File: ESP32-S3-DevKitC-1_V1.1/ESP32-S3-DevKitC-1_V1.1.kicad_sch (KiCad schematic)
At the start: 46 parts, among them IC1 SGM2212-3.3XKC3G_TR, J2 Conn_01x22, J3 Conn_01x22, P1 USB_C_Plug_USB2.0, Q3 L8050QLT1G, Q4 L8050QLT1G, SW1 NTC013-AT1J-A160T, SW2 NTC013-AT1J-A160T, U1 CP2102N-Axx-xQFN28, U4 ESP32-S3-WROOM-1, U5 AMS1117

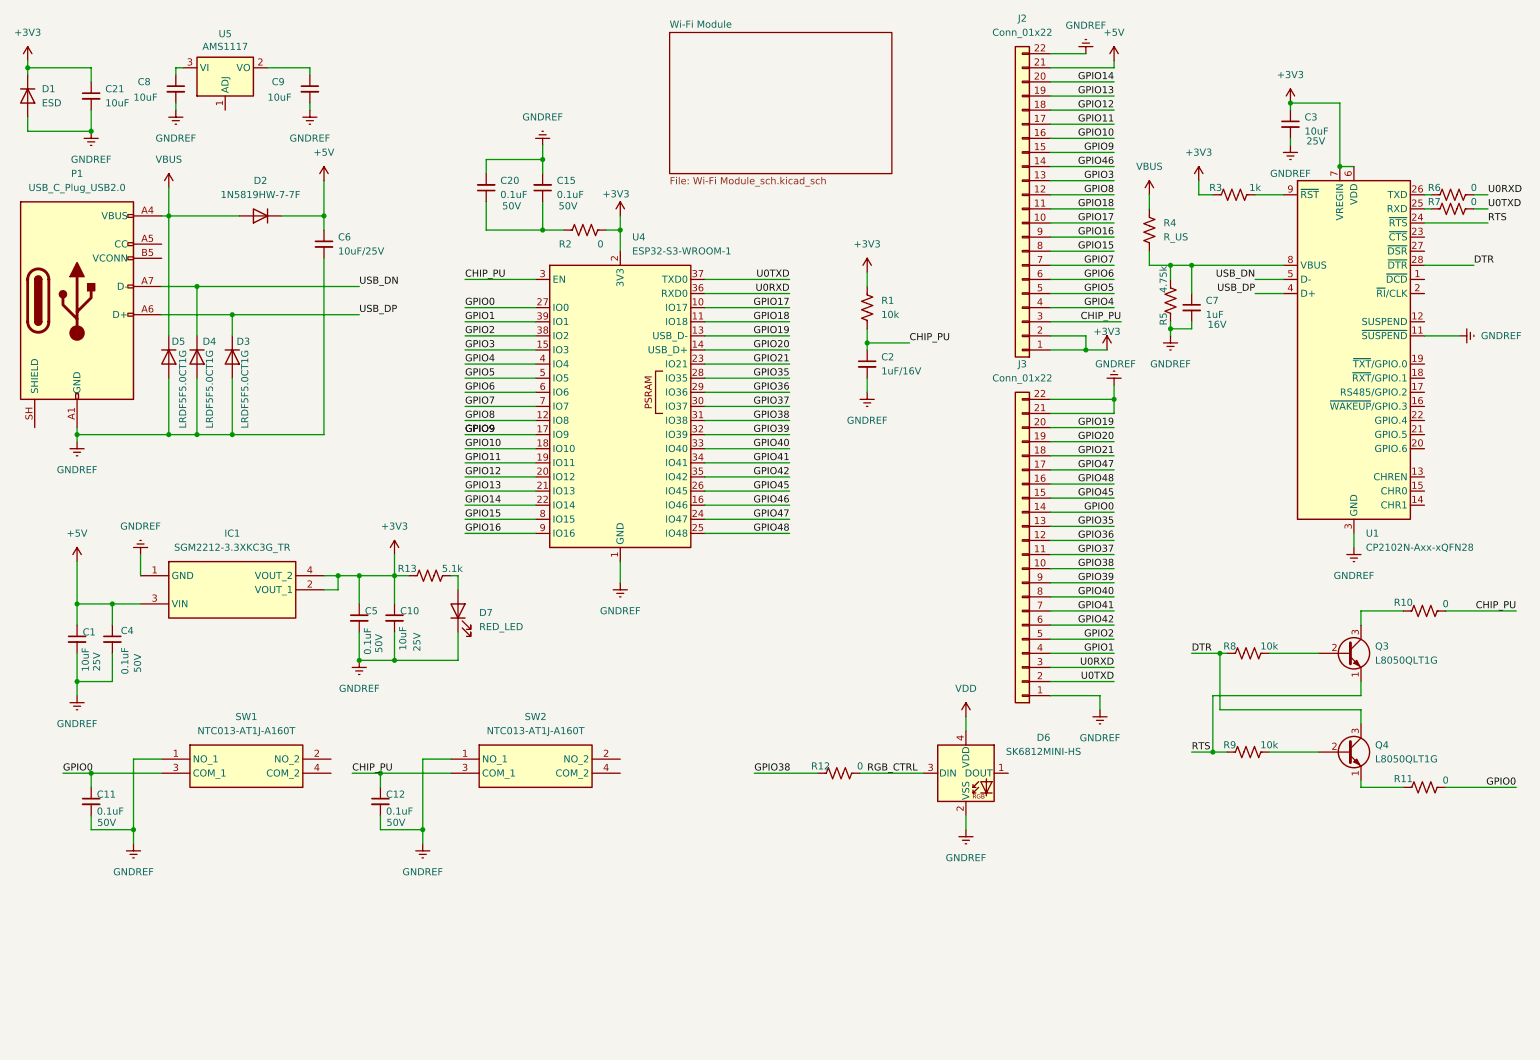
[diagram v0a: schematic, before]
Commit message: Update ESP32-S3-DevKitC-1_V1.1
I'm update the ESP32-S3-DevKitC-1_V1.1, include the sch and pcb layout.
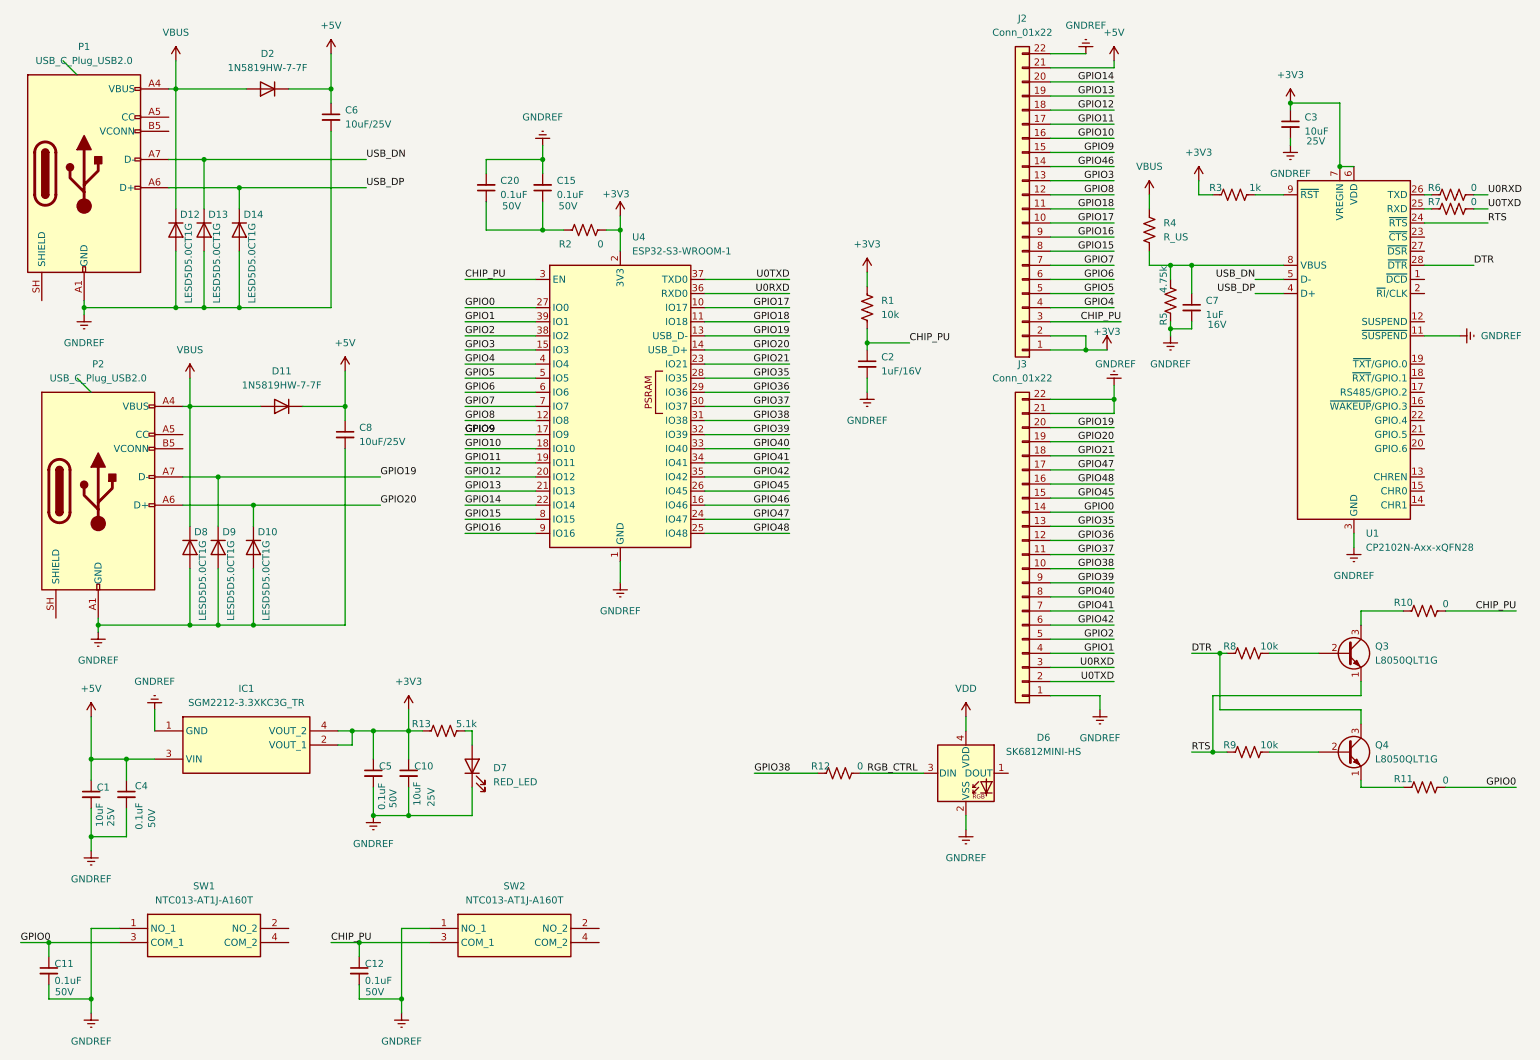
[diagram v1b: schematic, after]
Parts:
- removed C21, C9: 10uF, symbol Device:C_Small
- removed D1: ESD, symbol Device:D
- removed D3, D4, D5: LRDF5F5.0CT1G, symbol Device:D
- removed U5: AMS1117, Package_TO_SOT_SMD:SOT-223-3_TabPin2, symbol Regulator_Linear:AMS1117
- added D10, D12, D13, D14, D8, D9: LESD5D5.0CT1G, ESP32-S3-DevKitC-1_V1.1:LESD5D50CT1G, symbol Device:D
- added D11: 1N5819HW-7-7F, ESP32-S3-DevKitC-1_V1.1:SOD3716X145N, symbol Device:D
- added P2: USB_C_Plug_USB2.0, Connector_USB:USB_C_Receptacle_GCT_USB4135-GF-A_6P_TopMnt_Horizontal, symbol Connector:USB_C_Plug_USB2.0
- C1, C10, C11, C12, C15, C2, C20, C3, C4, C5, C6, C7: footprint (none) -> Capacitor_SMD:C_0603_1608Metric
- C8: value 10uF -> 10uF/25V; footprint (none) -> Capacitor_SMD:C_0603_1608Metric
- D2: footprint (none) -> ESP32-S3-DevKitC-1_V1.1:SOD3716X145N
- D7: footprint (none) -> LED_SMD:LED_0805_2012Metric
- J2, J3: footprint (none) -> Jumper:SolderJumper-2_P1.3mm_Open_RoundedPad1.0x1.5mm
- P1: footprint (none) -> Connector_USB:USB_C_Receptacle_GCT_USB4135-GF-A_6P_TopMnt_Horizontal
- Q3, Q4: footprint (none) -> ESP32-S3-DevKitC-1_V1.1:L8050QLT1G
- R1, R10, R11, R12, R13, R2, R3, R4, R5, R6, R7, R8, R9: footprint (none) -> Resistor_SMD:R_0603_1608Metric
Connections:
- net +5V: now also C8.1, D11.1 (K)
- net GNDREF: now also D10.2 (A), D12.2 (A), D13.2 (A), D14.2 (A), D8.2 (A), D9.2 (A), P2.A1 (GND), P2.A12 (GND), P2.B1 (GND), P2.B12 (GND)
- net GPIO19: now also D9.1 (K), P2.A7 (D-)
- net GPIO20: now also D10.1 (K), P2.A6 (D+)
- net USB_DN: now also D13.1 (K)
- net USB_DP: now also D14.1 (K)
- net VBUS: now also D11.2 (A), D12.1 (K), D8.1 (K), P2.A4 (VBUS), P2.A9 (VBUS), P2.B4 (VBUS), P2.B9 (VBUS)
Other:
- removed sheet Wi-Fi Module
- moved on the sheet: C1, C10, C11, C12, C4, C5, C6, D2, D7, IC1, P1, R13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

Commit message: New update
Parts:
- added C9: 0.1uF, Capacitor_SMD:C_0603_1608Metric, symbol Device:C_Small
- added R14, R15: 0, Resistor_SMD:R_0603_1608Metric, symbol Device:R_US
- added SW3, SW4: SW_Push, Tactile push button switch SMD SPST, symbol Switch:SW_Push
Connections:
- net GNDREF: now also C9.1, SW3.1
- net GPIO0: now also R15.1
- new net: C9.2, R14.1, SW3.2
- new net: R15.2, SW4.2
- new net EN: R14.2
- new net VCC: SW4.1

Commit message: update the ESP32 pcb layout
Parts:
- J3: value Conn_01x22 -> Conn01x02
- SW2: footprint NTC013AT1JA160T -> ESP32-S3-DevKitC-1_V1.1:NTC013AT1JA160T
- SW3, SW4: footprint Tactile push button switch SMD SPST -> Button_Switch_SMD:SW_SPST_Omron_B3FS-100xP
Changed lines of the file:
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@@
 		(color 0 0 0 0)
 	)
-	(bus_entry
-		(at 21.59 20.32)
-		(size 2.54 2.54)
-		(stroke
-			(width 0)
-			(type default)
-		)
-	)
-	(bus_entry
-		(at 24.13 77.47)
-		(size 2.54 2.54)
-		(stroke
-			(width 0)
-			(type default)
-		)
-	)
 	(wire
 		(pts
@@
 			)
 		)
-		(property "Footprint" "Tactile push button switch SMD SPST"
+		(property "Footprint" "Button_Switch_SMD:SW_SPST_Omron_B3FS-100xP"
 			(at 120.65 128.27 0)
 			(hide yes)
@@
 			)
 		)
-		(property "Footprint" "NTC013AT1JA160T"
+		(property "Footprint" "ESP32-S3-DevKitC-1_V1.1:NTC013AT1JA160T"
 			(at 114.3 271.45 0)
 			(hide yes)
@@
 			)
 		)
-		(property "Value" "Conn_01x22"
+		(property "Value" "Conn01x02"
 			(at 194.31 77.47 0)
 			(show_name no)
@@
 			)
 		)
-		(property "Footprint" "Tactile push button switch SMD SPST"
+		(property "Footprint" "Button_Switch_SMD:SW_SPST_Omron_B3FS-100xP"
 			(at 80.01 58.42 0)
 			(hide yes)
